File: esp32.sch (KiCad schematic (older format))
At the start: 1 part, among them U2 ESP32-DEVKITC

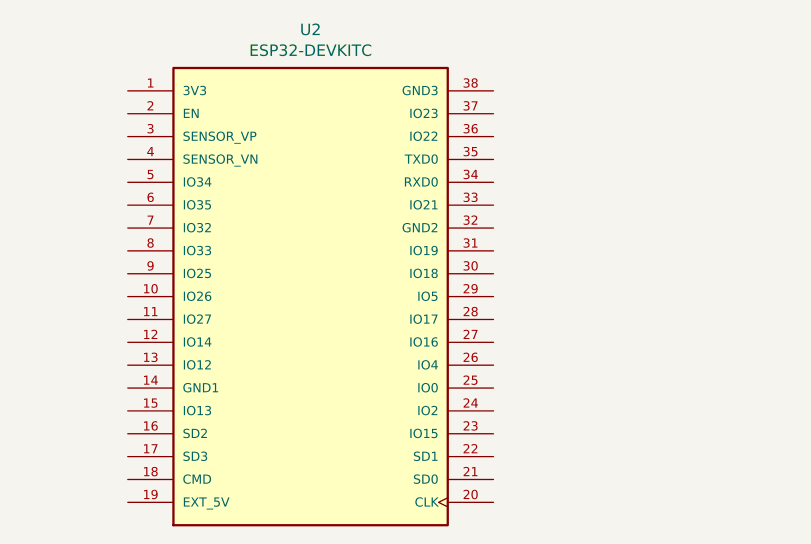
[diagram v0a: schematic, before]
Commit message: batt_alim module added
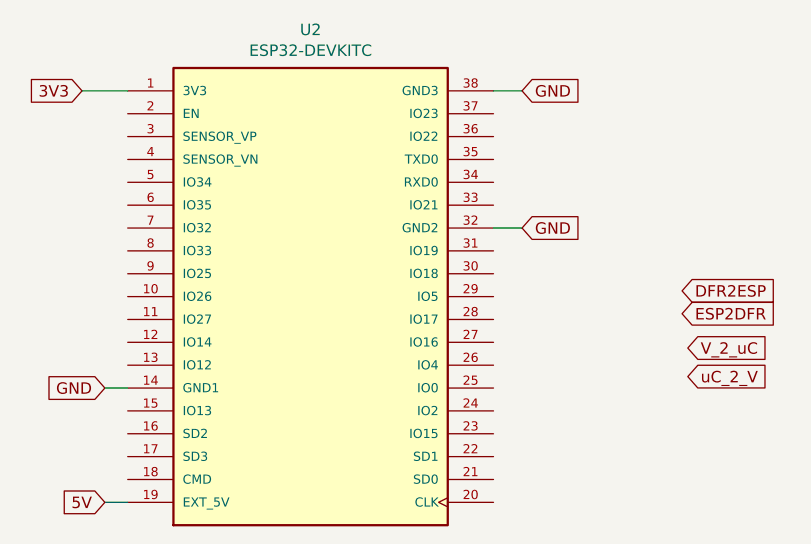
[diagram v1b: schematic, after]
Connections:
- net 3V3: now reaches U2.1 (3V3)
- net GND: now reaches U2.14 (GND1)
- net GND: now also U2.32 (GND2), U2.38 (GND3)
- net 5V: now reaches U2.19 (EXT_5V)
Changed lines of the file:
@@
 	1    0    0    -1
 $EndComp
+Text GLabel 7825 2625 2    50   Input ~ 0
+GND
+Text GLabel 6000 4425 0    50   Input ~ 0
+5V
+Text GLabel 8525 3600 2    50   Input ~ 0
+ESP2DFR
+Text GLabel 8525 3500 2    50   Input ~ 0
+DFR2ESP
+Text GLabel 6000 3925 0    50   Input ~ 0
+GND
+Text GLabel 7825 3225 2    50   Input ~ 0
+GND
+Text GLabel 8550 3750 2    50   Input ~ 0
+V_2_uC
+Text GLabel 8550 3875 2    50   Input ~ 0
+uC_2_V
+Text GLabel 5900 2625 0    50   Input ~ 0
+3V3
+Wire Wire Line
+	5900 2625 6100 2625
+Wire Wire Line
+	6000 4425 6100 4425
+Wire Wire Line
+	7700 2625 7825 2625
+Wire Wire Line
+	6000 3925 6100 3925
+Wire Wire Line
+	7700 3225 7825 3225
 $EndSCHEMATC

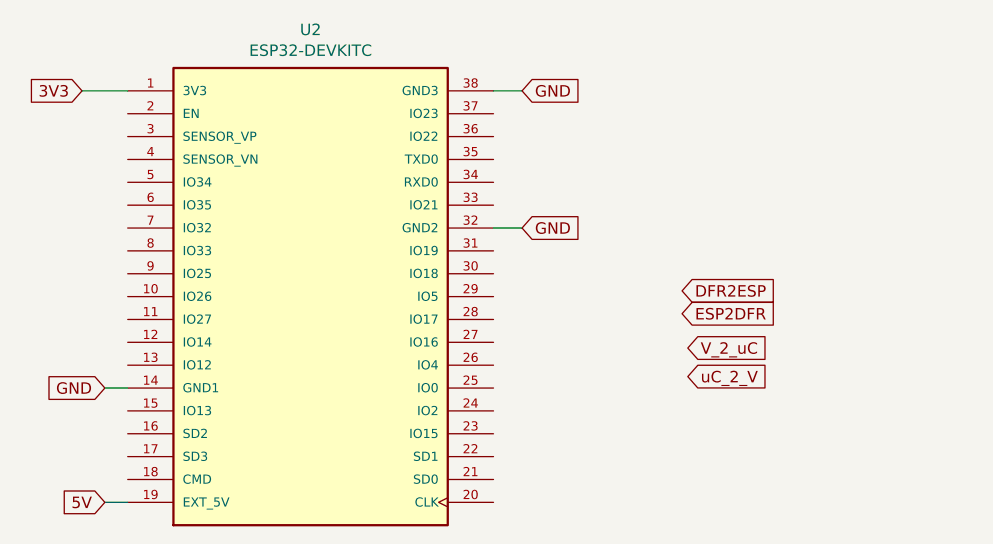
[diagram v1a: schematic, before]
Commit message: added battery footprint
and some net names
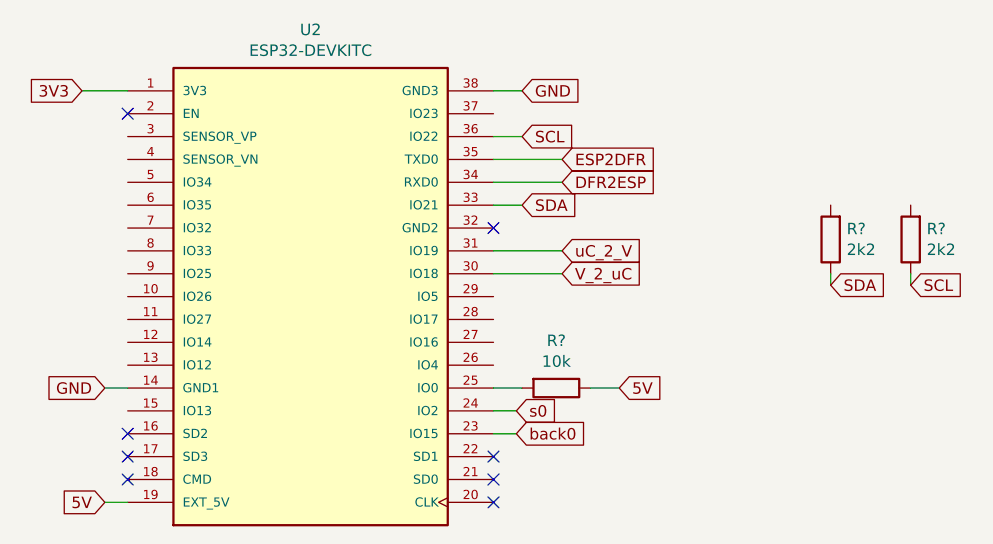
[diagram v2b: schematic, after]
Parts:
- added R?: 10k, Resistor_SMD:R_0603_1608Metric_Pad1.05x0.95mm_HandSolder, symbol Device:R
- added R? (x2): 2k2, Resistor_SMD:R_0603_1608Metric_Pad1.05x0.95mm_HandSolder, symbol Device:R
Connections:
- net 5V: now also R?.1
- net DFR2ESP: now also U2.34 (RXD0)
- net ESP2DFR: now also U2.35 (TXD0)
- net GND: no longer U2.32 (GND2)
- net V_2_uC: now also U2.30 (IO18)
- net uC_2_V: now also U2.31 (IO19)
- net back0: now reaches U2.23 (IO15)
- net s0: now reaches U2.24 (IO2)
- net at U2.25 (IO0): now also R?.2
- net SDA: now reaches U2.33 (IO21)
- net SDA: now also R?.1
- net SCL: now reaches U2.36 (IO22)
- net SCL: now also R?.1
- no-connect marks 0 -> 8
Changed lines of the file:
@@
 Text GLabel 6000 4425 0    50   Input ~ 0
 5V
-Text GLabel 8525 3600 2    50   Input ~ 0
+Text GLabel 8000 2925 2    50   Input ~ 0
 ESP2DFR
-Text GLabel 8525 3500 2    50   Input ~ 0
+Text GLabel 8000 3025 2    50   Input ~ 0
 DFR2ESP
 Text GLabel 6000 3925 0    50   Input ~ 0
 GND
-Text GLabel 7825 3225 2    50   Input ~ 0
-GND
-Text GLabel 8550 3750 2    50   Input ~ 0
+Text GLabel 8000 3425 2    50   Input ~ 0
 V_2_uC
-Text GLabel 8550 3875 2    50   Input ~ 0
+Text GLabel 8000 3325 2    50   Input ~ 0
 uC_2_V
 Text GLabel 5900 2625 0    50   Input ~ 0
@@
 Wire Wire Line
 	6000 3925 6100 3925
+NoConn ~ 6100 2725
+NoConn ~ 7700 4225
+NoConn ~ 7700 4425
+NoConn ~ 7700 4325
+NoConn ~ 6100 4125
+NoConn ~ 6100 4225
+NoConn ~ 6100 4325
+NoConn ~ 7700 3225
+$Comp
+L Device:R R?
+U 1 1 5FDF84F4
+P 7975 3925
+F 0 "R?" V 7768 3925 50  0000 C CNN
+F 1 "10k" V 7859 3925 50  0000 C CNN
+F 2 "Resistor_SMD:R_0603_1608Metric_Pad1.05x0.95mm_HandSolder" V 7905 3925 50  0001 C CNN
+F 3 "~" H 7975 3925 50  0001 C CNN
+	1    7975 3925
+	0    1    1    0
+$EndComp
+Text GLabel 8250 3925 2    50   Input ~ 0
+5V
 Wire Wire Line
-	7700 3225 7825 3225
+	7700 3925 7825 3925
+Wire Wire Line
+	8125 3925 8250 3925
+Wire Wire Line
+	7700 2925 8000 2925
+Wire Wire Line
+	7700 3025 8000 3025
+Wire Wire Line
+	7700 3325 8000 3325
+Wire Wire Line
+	7700 3425 8000 3425
+Text GLabel 7825 3125 2    50   Input ~ 0
+SDA
+Text GLabel 7825 2825 2    50   Input ~ 0
+SCL
+Wire Wire Line
+	7700 2825 7825 2825
+Wire Wire Line
+	7700 3125 7825 3125
+$Comp
+L Device:R R?
+U 1 1 5FDFA2E8
+P 9175 3275
+F 0 "R?" H 9105 3229 50  0000 R CNN
+F 1 "2k2" H 9105 3320 50  0000 R CNN
+F 2 "Resistor_SMD:R_0603_1608Metric_Pad1.05x0.95mm_HandSolder" V 9105 3275 50  0001 C CNN
+F 3 "~" H 9175 3275 50  0001 C CNN
+	1    9175 3275
+	-1   0    0    1
+$EndComp
+$Comp
+L Device:R R?
+U 1 1 5FDFA6EA
+P 9525 3275
+F 0 "R?" H 9455 3229 50  0000 R CNN
+F 1 "2k2" H 9455 3320 50  0000 R CNN
+F 2 "Resistor_SMD:R_0603_1608Metric_Pad1.05x0.95mm_HandSolder" V 9455 3275 50  0001 C CNN
+F 3 "~" H 9525 3275 50  0001 C CNN
+	1    9525 3275
+	-1   0    0    1
+$EndComp
+Text GLabel 9525 3475 2    50   Input ~ 0
+SCL
+Text GLabel 9175 3475 2    50   Input ~ 0
+SDA
+Wire Wire Line
+	9175 3425 9175 3475
+Wire Wire Line
+	9525 3425 9525 3475
+Text GLabel 7800 4025 2    50   Input ~ 0
+s0
+Text GLabel 7800 4125 2    50   Input ~ 0
+back0
+Wire Wire Line
+	7700 4025 7800 4025
+Wire Wire Line
+	7700 4125 7800 4125
 $EndSCHEMATC

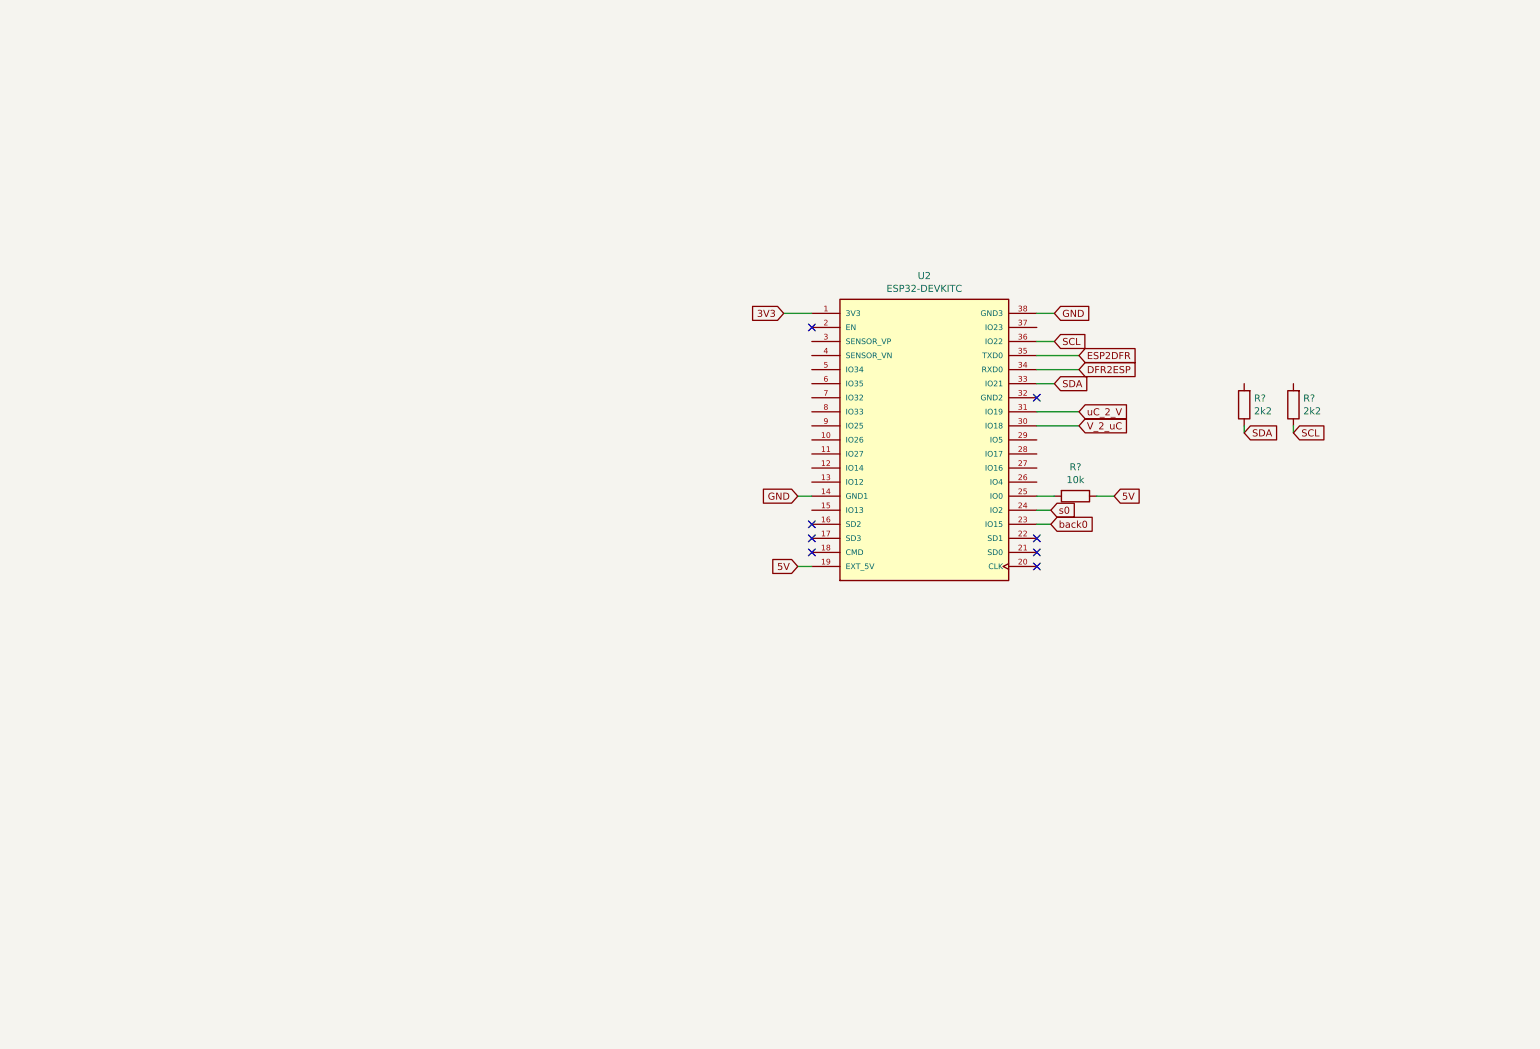
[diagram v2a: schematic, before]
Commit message: fin schéma, début placement
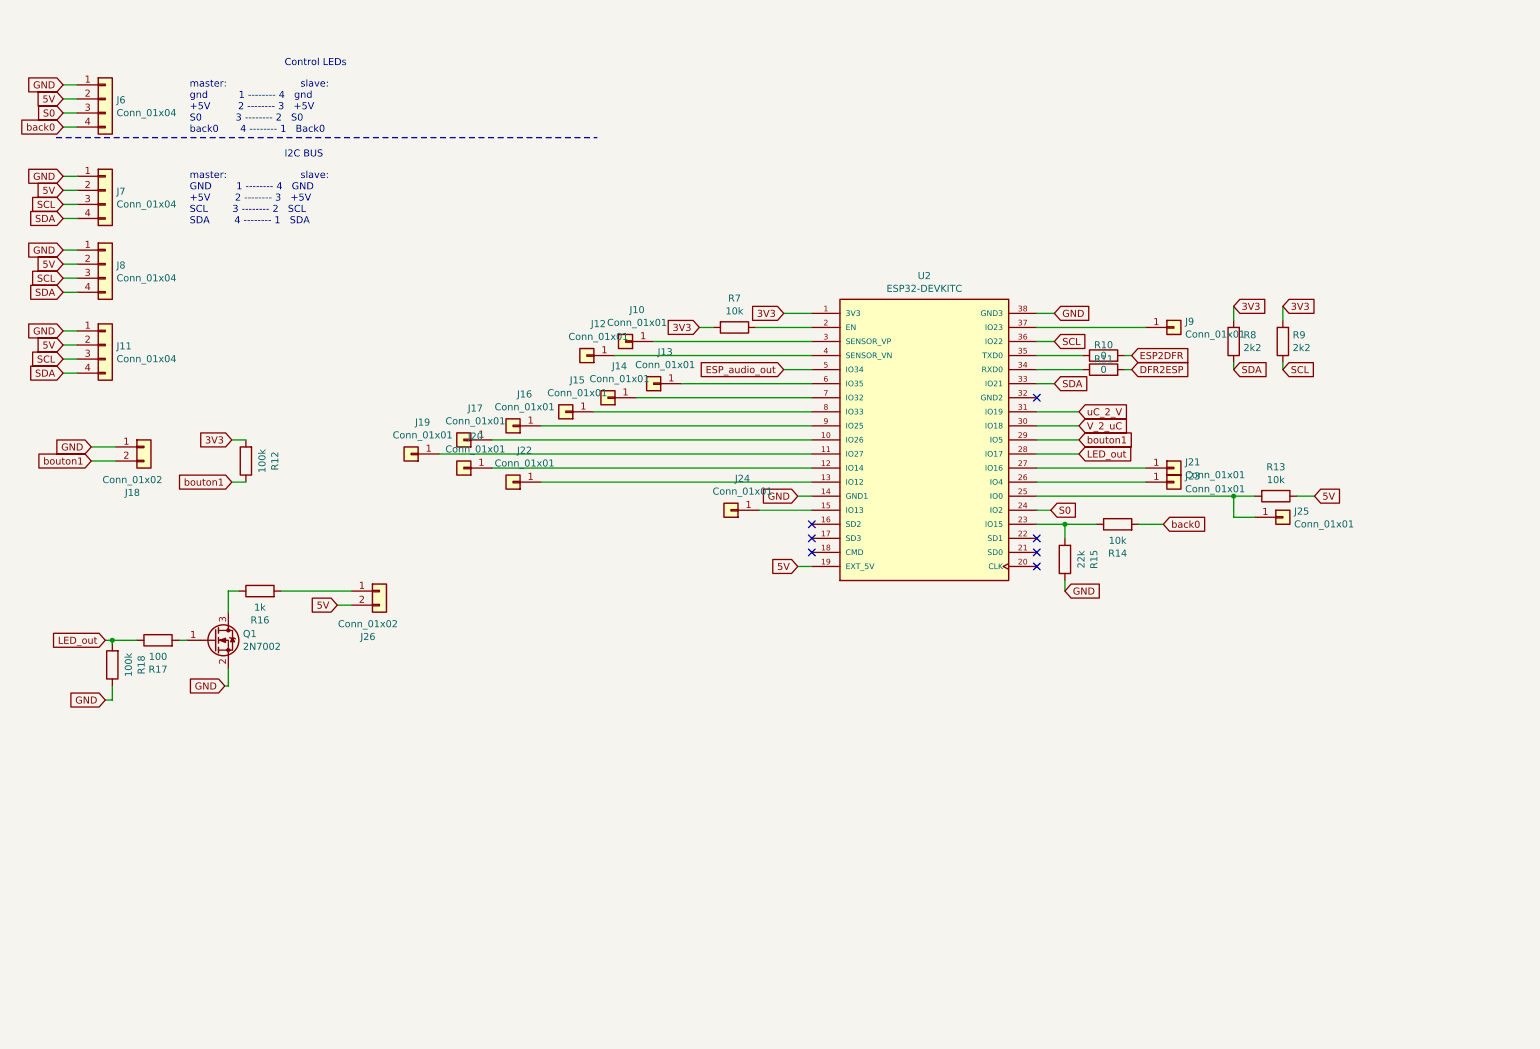
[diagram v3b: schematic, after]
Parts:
- added J10, J12, J13, J14, J15, J16, J17, J19, J20, J21, J22, J23, J24, J25, J9: Conn_01x01, Connector_PinHeader_2.54mm:PinHeader_1x01_P2.54mm_Vertical, symbol Connector_Generic:Conn_01x01
- added J11, J6, J7, J8: Conn_01x04, Connector_JST:JST_XH_B4B-XH-A_1x04_P2.50mm_Vertical, symbol Connector_Generic:Conn_01x04
- added J18, J26: Conn_01x02, Connector_JST:JST_XH_B2B-XH-A_1x02_P2.50mm_Vertical, symbol Connector_Generic:Conn_01x02
- added Q1: 2N7002, Package_TO_SOT_SMD:SOT-23, symbol Transistor_FET:2N7002
- added R10, R11: 0, Resistor_SMD:R_0603_1608Metric_Pad1.05x0.95mm_HandSolder, symbol Device:R
- added R12, R18: 100k, Resistor_SMD:R_0603_1608Metric_Pad1.05x0.95mm_HandSolder, symbol Device:R
- added R14, R7: 10k, Resistor_SMD:R_0603_1608Metric_Pad1.05x0.95mm_HandSolder, symbol Device:R
- added R15: 22k, Resistor_SMD:R_0603_1608Metric_Pad1.05x0.95mm_HandSolder, symbol Device:R
- added R16: 1k, Resistor_SMD:R_0603_1608Metric_Pad1.05x0.95mm_HandSolder, symbol Device:R
- added R17: 100, Resistor_SMD:R_0603_1608Metric_Pad1.05x0.95mm_HandSolder, symbol Device:R
- gave numbers to parts that had none: 3
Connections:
- net 3V3: now also R8.2, R9.2, R12.2, R7.2
- net 5V: now also J11.2 (Pin_2), J26.2 (Pin_2), J6.2 (Pin_2), J7.2 (Pin_2), J8.2 (Pin_2)
- net DFR2ESP: now also R11.2; no longer U2.34 (RXD0)
- net ESP2DFR: now also R10.2; no longer U2.35 (TXD0)
- net GND: now also J11.1 (Pin_1), J18.1 (Pin_1), J6.1 (Pin_1), J7.1 (Pin_1), J8.1 (Pin_1), Q1.2 (S), R15.1, R18.1
- net SCL: now also J11.3 (Pin_3), J7.3 (Pin_3), J8.3 (Pin_3)
- net SDA: now also J11.4 (Pin_4), J7.4 (Pin_4), J8.4 (Pin_4)
- net back0: now also J6.4 (Pin_4), R14.2; no longer U2.23 (IO15)
- net at U2.10 (IO26): now also J17.1 (Pin_1)
- net at U2.11 (IO27): now also J19.1 (Pin_1)
- net at U2.12 (IO14): now also J20.1 (Pin_1)
- net at U2.13 (IO12): now also J22.1 (Pin_1)
- net at U2.15 (IO13): now also J24.1 (Pin_1)
- net at U2.2 (EN): now also R7.1
- net at R13.2, U2.25 (IO0): now also J25.1 (Pin_1)
- net at U2.26 (IO4): now also J23.1 (Pin_1)
- net at U2.27 (IO16): now also J21.1 (Pin_1)
- net LED_out: now reaches U2.28 (IO17)
- net LED_out: now also R17.1, R18.2
- net bouton1: now reaches U2.29 (IO5)
- net bouton1: now also J18.2 (Pin_2), R12.1
- net at U2.3 (SENSOR_VP): now also J10.1 (Pin_1)
- net at U2.37 (IO23): now also J9.1 (Pin_1)
- net at U2.4 (SENSOR_VN): now also J12.1 (Pin_1)
- net ESP_audio_out: now reaches U2.5 (IO34)
- net at U2.6 (IO35): now also J13.1 (Pin_1)
- net at U2.7 (IO32): now also J14.1 (Pin_1)
- net at U2.8 (IO33): now also J15.1 (Pin_1)
- net at U2.9 (IO25): now also J16.1 (Pin_1)
- net s0 renamed S0
- net S0: now also J6.3 (Pin_3)
- new net: R14.1, R15.2, U2.23 (IO15)
- new net: R11.1, U2.34 (RXD0)
- new net: R10.1, U2.35 (TXD0)
- new net: J26.1 (Pin_1), R16.2
- new net: Q1.1 (G), R17.2
- new net: Q1.3 (D), R16.1
- no-connect marks 8 -> 7
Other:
- note added: "Control LEDs"
- note added: "I2C BUS"
- note added: "master: slave:\nGND 1 -------- 4 GND\n+5V 2 -------- 3 +5V\nSCL 3 -------- 2 SCL\nSDA 4 -------- 1 SDA"
- note added: "master: slave:\ngnd 1 -------- 4 gnd\n+5V 2 -------- 3 +5V\nS0 3 -------- 2 S0\nback0 4 -------- 1 Back0"
- moved on the sheet: R13, R8, R9
